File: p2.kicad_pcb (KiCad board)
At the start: 2 copper layers, 66 x 57 mm, 34 parts, among them J1 BARREL_JACK, J2 FLASH_JMP, J3 UART, J4 ALT_POWER, J5 jack-3.5mm-5pin, J6 jack-3.5mm-5pin, J7 jack-3.5mm-5pin, J8 jack-3.5mm-5pin, Q1 IRL540N, Q2 IRL540N, U1 LM1117IMP-33, U2 ESP-12F

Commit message: current state sync
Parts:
- removed C1: 10uF, Capacitors_THT:CP_Radial_Tantal_D5.0mm_P2.50mm
- removed R1, R2, R6, R7: 10k, Resistors_THT:R_Axial_DIN0207_L6.3mm_D2.5mm_P7.62mm_Horizontal
- added LED1: LED, LEDs:LED_D3.0mm_Horizontal_O1.27mm_Z2.0mm, F.Cu at (59.2, 27.6)
- added LED2: LED, LEDs:LED_D3.0mm_Horizontal_O1.27mm_Z2.0mm, F.Cu at (54.1, 27.6)
- added R8: 1k, Resistors_THT:R_Axial_DIN0207_L6.3mm_D2.5mm_P7.62mm_Horizontal, F.Cu at (51.6, 37.8)
- added R9: 1k, Resistors_THT:R_Axial_DIN0207_L6.3mm_D2.5mm_P7.62mm_Horizontal, F.Cu at (54.1, 37.8)
- added RN1: 10k, Resistors_THT:R_Array_SIP5, F.Cu at (38.3, 52.3)
- added U3: Switch, Buttons_Switches_THT:SW_PUSH_6mm, F.Cu at (68.5, 27.1)
- C2: value 10uF -> 10u
- C3, C4: value 100nF -> 100n
- U1: value LM1117IMP-33 -> R-78E3.3-0.5; footprint TO_SOT_Packages_SMD:SOT-223 -> myfootprints:DCDC-Conv_Recom_R-78Exx-0.5
- U2: value ESP-12F -> ESP-12; footprint esp8266:ESP-12E -> esp8266:ESP-12
- moved REF*** 26.7 mm to (68.1, 59.9)
- moved C2 15.9 mm to (42.4, 48.3), turned to 0 degrees
- moved U1 11.7 mm to (53.6, 45.7)
- moved G*** 5.67 mm to (70.6, 39.3)
- moved REF** 5.60 mm to (71.7, 41.6)
- moved J1 1.70 mm to (38.1, 26.0)
- moved J3 1.27 mm to (45.2, 74.6)
- moved R5 1.13 mm to (77.1, 74.6)
- moved R3 1.08 mm to (35.1, 74.6)
- moved REF** 1.08 mm to (38.0, 35.5)
- moved C3 0.63 mm to (33.8, 47.3)
- moved C4 0.63 mm to (55.4, 51.1)
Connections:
- net Net-(D1-Pad2) renamed /pump1
- net Net-(D2-Pad2) renamed /pump2
- net Net-(R3-Pad2) renamed /wifi-sw
- C2 pad 1: /Vcc -> +3V3
- C3 pad 2: /Vcc -> +3V3
- D1 pad 1: /12V -> +12V
- D2 pad 1: /12V -> +12V
- J1 pad 1: /12V -> +12V
- J3 pad 2: /Vcc -> +3V3
- J4 pad 2: /12V -> +12V
- J7 pad 2: /12V -> +12V
- J8 pad 2: /12V -> +12V
- U1 pad 1: GNDREF -> +12V
- U1 pad 2: /Vcc -> GNDREF
- U1 pad 3: /12V -> +3V3
- U2 pad 13: Net-(U2-Pad13) -> /led2
- U2 pad 14: Net-(U2-Pad14) -> /led1
- U2 pad 8: /Vcc -> +3V3
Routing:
- net /12V: track 134.5 -> 0.00 mm
- net +3V3: track 0.00 -> 117.3 mm
- net +12V: track 0.00 -> 100.3 mm
- net /Vcc: track 75.4 -> 0.00 mm
- net /wifi-sw: track 8.12 -> 76.1 mm, vias 0 -> 2
- net /led1: track 0.00 -> 53.4 mm, vias 0 -> 1
- net /led2: track 0.00 -> 47.6 mm, vias 0 -> 1
- net /ctl1: track 64.0 -> 71.0 mm
- net /pump2: track 21.9 -> 16.3 mm
- net GNDREF: track 4.50 -> 0.54 mm
- net Net-(LED1-Pad2): track 0.00 -> 3.59 mm
- net /ctl2: track 59.5 -> 56.7 mm
- net Net-(LED2-Pad2): track 0.00 -> 2.54 mm
- net Net-(Q1-Pad1): track 36.2 -> 38.6 mm
- net /GPIO0: track 24.0 -> 22.1 mm
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- removed copper zone on F.Cu, net /HEAT_Vcc
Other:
- outline, holes or cut-outs redrawn
- board text added: "Gnd"
- board text added: "GndVcc Rx Tx"
- board text added: "Pump1"
- board text added: "Pump2"
- board text added: "Sensor1"
- board text added: "Sensor2"
- board text added: "WaterControl v2 r1.7"
- board text added: "short"
- board text added: "to flash"
- board text removed: "GND"
- board text removed: "Short to flash"
- board text removed: "WaterControl v2 r1.1"

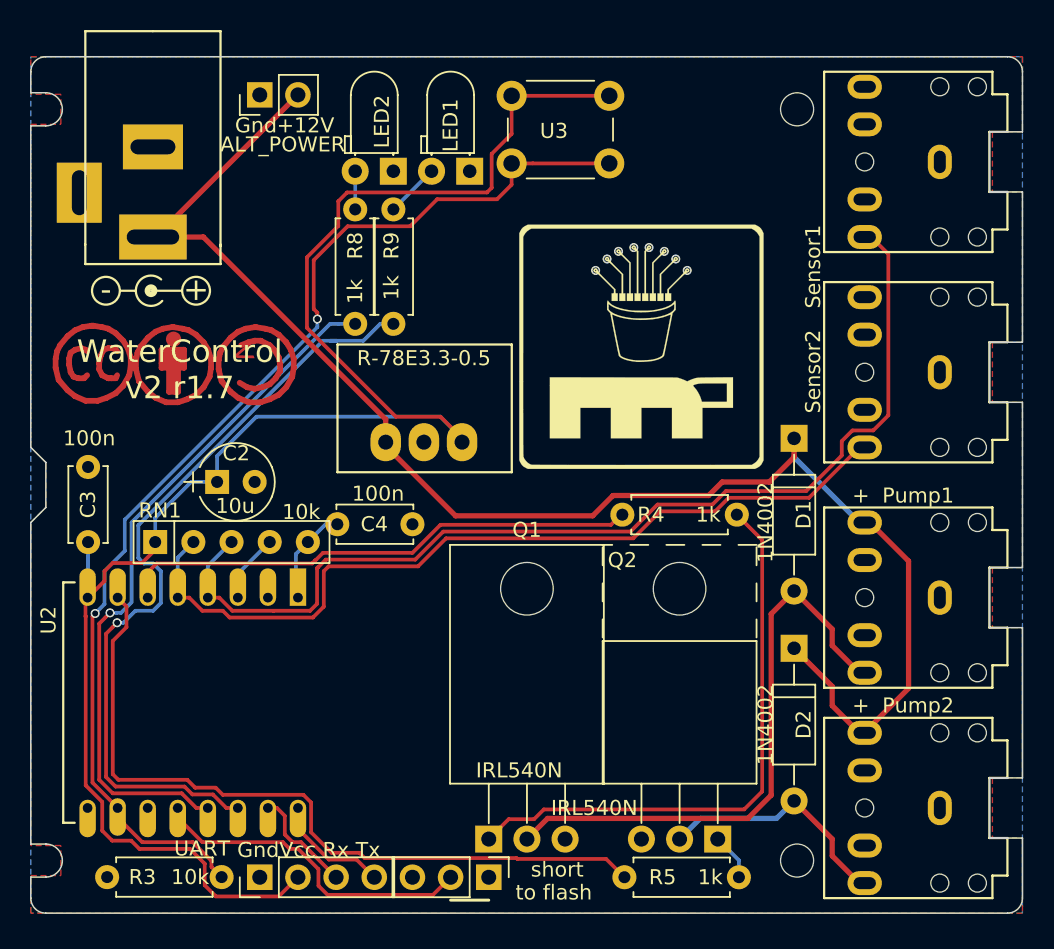
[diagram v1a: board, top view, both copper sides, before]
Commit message: rev4.1 - switched to capacitive sensors by including a multiplexer, added another switch, rotated both.
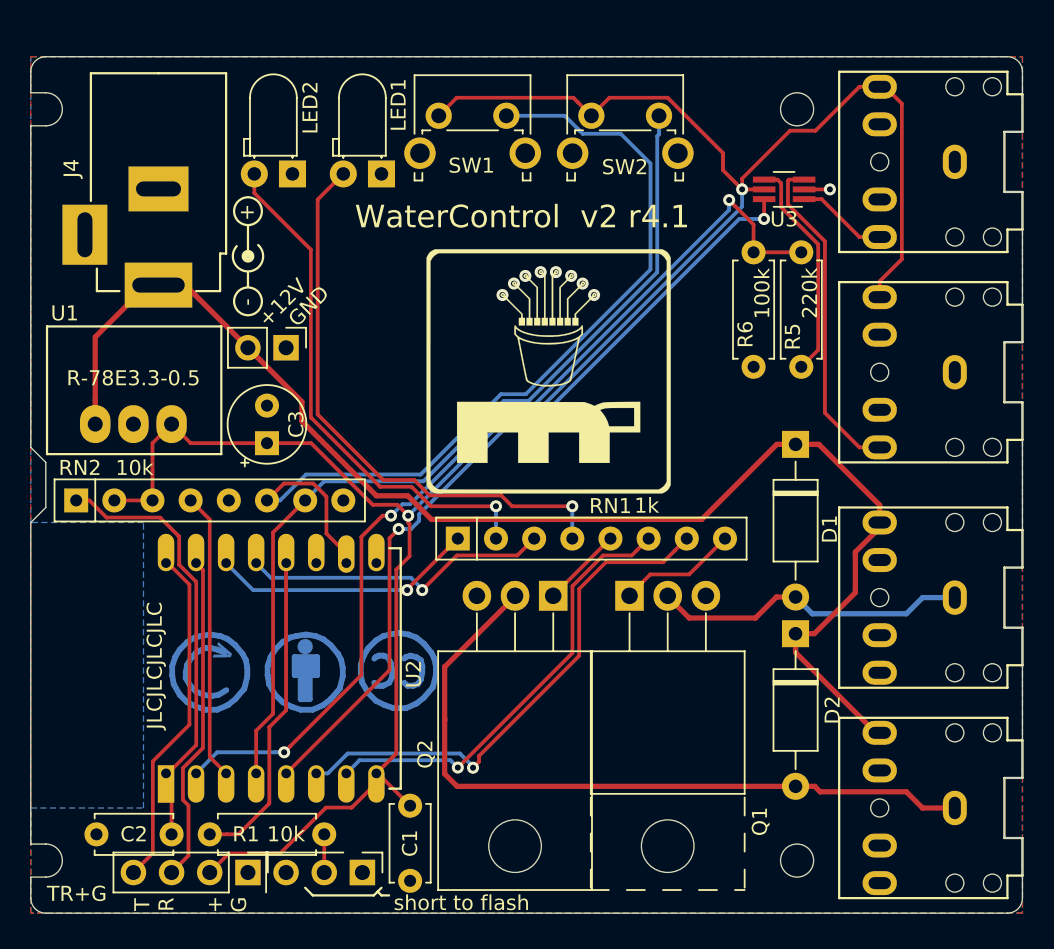
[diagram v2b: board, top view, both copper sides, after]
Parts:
- removed C4: 100n, Capacitors_THT:C_Disc_D5.0mm_W2.5mm_P5.00mm
- removed the G*** at (70.6, 39.3)
- removed R3: 10k, Resistors_THT:R_Axial_DIN0207_L6.3mm_D2.5mm_P7.62mm_Horizontal
- removed R4, R8, R9: 1k, Resistors_THT:R_Axial_DIN0207_L6.3mm_D2.5mm_P7.62mm_Horizontal
- removed the REF** at (34.0, 40.5)
- removed the REF** at (45.0, 40.5)
- removed the REF** at (39.5, 40.5)
- removed the REF** at (71.7, 41.6)
- removed the REF** at (38.0, 35.5)
- removed REF***: OSHW-Logo2_9.8x8mm_SilkScreen, Symbols:OSHW-Logo2_9.8x8mm_SilkScreen
- added C1: 100n, Capacitor_THT:C_Disc_D5.0mm_W2.5mm_P5.00mm, F.Cu at (55.2, 69.8)
- added G***: MR_EDGE_PCBPOT, mylogos:mr_edge_pcbpot, B.Cu at (64.5, 40.9)
- added G***: MR_EDGE_PCBPOT, mylogos:mr_edge_pcbpot, F.Cu at (64.5, 40.9)
- added R1: 10k, Resistor_THT:R_Axial_DIN0207_L6.3mm_D2.5mm_P7.62mm_Horizontal, F.Cu at (41.9, 71.8)
- added R6: 100k, Resistor_THT:R_Axial_DIN0207_L6.3mm_D2.5mm_P7.62mm_Horizontal, F.Cu at (78.1, 40.6)
- added REF**: Symbol_Barrel_Polarity, Symbol:Symbol_Barrel_Polarity, F.Cu at (44.4, 33.3)
- added REF**: Symbol_CC-ShareAlike_CopperTop_Small, Symbol:Symbol_CC-ShareAlike_CopperTop_Small, B.Cu at (41.9, 61.0)
- added REF**: Symbol_CC-Attribution_CopperTop_Small, Symbol:Symbol_CC-Attribution_CopperTop_Small, B.Cu at (48.3, 61.0)
- added REF**: Symbol_CreativeCommons_CopperTop_Type2_Small, Symbol:Symbol_CreativeCommons_CopperTop_Type2_Small, B.Cu at (54.6, 61.0)
- added REF**: OSHW-Logo2_9.8x8mm_SilkScreen, Symbol:OSHW-Logo2_9.8x8mm_SilkScreen, B.Cu at (46.5, 33.7)
- added RN2: 10k, myfootprints:ResistorArrayx4-18726345, F.Cu at (33.0, 49.5)
- added SW1: SW_Push, Button_Switch_THT:SW_Tactile_SPST_Angled_PTS645Vx58-2LFS, F.Cu at (57.1, 23.9)
- added SW2: SW_Push, Button_Switch_THT:SW_Tactile_SPST_Angled_PTS645Vx58-2LFS, F.Cu at (67.3, 23.9)
- C2: value 10u -> 100n; footprint Capacitors_THT:CP_Radial_Tantal_D5.0mm_P2.50mm -> Capacitor_THT:C_Disc_D5.0mm_W2.5mm_P5.00mm
- C3: value 100n -> 10u; footprint Capacitors_THT:C_Disc_D5.0mm_W2.5mm_P5.00mm -> Capacitor_THT:CP_Radial_Tantal_D5.0mm_P2.50mm
- D1, D2: footprint Diodes_THT:D_A-405_P10.16mm_Horizontal -> Diode_THT:D_A-405_P10.16mm_Horizontal
- J1: value BARREL_JACK -> FLASH_JMP; footprint myfootprints:Barrel_Jack_5.5_2.1mm -> myfootprints:PinHeader_2.54mm_1x3_short
- J2: value FLASH_JMP -> UART; footprint Pin_Headers:Pin_Header_Straight_1x03_Pitch2.54mm -> Connector_PinHeader_2.54mm:PinHeader_1x04_P2.54mm_Vertical
- J3: value UART -> ALT_Pwr; footprint Pin_Headers:Pin_Header_Straight_1x04_Pitch2.54mm -> Connector_PinHeader_2.54mm:PinHeader_1x02_P2.54mm_Vertical
- J4: value ALT_POWER -> BARREL_JACK; footprint Pin_Headers:Pin_Header_Straight_1x02_Pitch2.54mm -> myfootprints:Barrel_Jack_5.5_2.1mm
- LED1, LED2: footprint LEDs:LED_D3.0mm_Horizontal_O1.27mm_Z2.0mm -> LED_THT:LED_D3.0mm_Horizontal_O1.27mm_Z2.0mm_Clear
- Q1: footprint TO_SOT_Packages_THT:TO-220_Horizontal -> Package_TO_SOT_THT:TO-220-3_Horizontal_TabUp
- Q2: footprint TO_SOT_Packages_THT:TO-220_Horizontal_Reversed -> Package_TO_SOT_THT:TO-220-3_Horizontal_TabDown
- R5: value 1k -> 220k; footprint Resistors_THT:R_Axial_DIN0207_L6.3mm_D2.5mm_P7.62mm_Horizontal -> Resistor_THT:R_Axial_DIN0207_L6.3mm_D2.5mm_P7.62mm_Horizontal
- RN1: value 10k -> 1k; footprint Resistors_THT:R_Array_SIP5 -> myfootprints:ResistorArrayx4-27185436
- U2: footprint esp8266:ESP-12 -> ESP8266:ESP-12
- U3: value Switch -> 74LVC1G3157; footprint Buttons_Switches_THT:SW_PUSH_6mm -> Package_TO_SOT_SMD:SOT-363_SC-70-6_Handsoldering
- moved J1 50.3 mm to (52.1, 74.3)
- moved R5 41.8 mm to (81.3, 33.0), turned to 270 degrees
- moved J3 35.3 mm to (47.0, 39.4), turned to 270 degrees
- moved C2 23.6 mm to (39.4, 71.8), turned to 180 degrees
- moved RN1 20.1 mm to (58.4, 52.1)
- moved Q2 19.5 mm to (64.8, 55.9)
- moved U1 19.4 mm to (34.3, 44.5)
- moved Q1 18.7 mm to (69.8, 55.9)
- moved J2 16.0 mm to (44.5, 74.3)
- moved U2 14.6 mm to (39.0, 67.7), turned to 90 degrees
- moved J5 14.0 mm to (91.5, 41.0)
- moved J6 14.0 mm to (91.5, 27.0)
- moved C3 12.0 mm to (45.7, 45.7), turned to 90 degrees
- moved U3 11.8 mm to (80.1, 28.8)
- moved J4 9.20 mm to (38.5, 28.8), turned to 270 degrees
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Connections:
- C2 pad 1: +3V3 -> /10k_to_3v3_1
- C2 pad 2: GNDREF -> GND
- C3 pad 1: GNDREF -> +3V3
- C3 pad 2: +3V3 -> GND
- D1 pad 2: /pump1 -> Net-(D1-Pad2)
- D2 pad 2: /pump2 -> Net-(D2-Pad2)
- J1 pad 1: +12V -> GND
- J1 pad 2: GNDREF -> Net-(J1-Pad2)
- J2 pad 1: GNDREF -> GND
- J2 pad 2: /GPIO0 -> +3V3
- J2 pad 3: Net-(J2-Pad3) -> /RXD0
- J3 pad 1: GNDREF -> GND
- J3 pad 2: +3V3 -> +12V
- J4 pad 1: GNDREF -> +12V
- J4 pad 2: +12V -> Net-(J4-Pad2)
- J5 pad 1: Net-(J5-Pad1) -> GND
- J5 pad 2: GNDREF -> +3V3
- J5 pad 3: /ctl1 -> Net-(J5-Pad3)
- J6 pad 1: Net-(J6-Pad1) -> GND
- J6 pad 2: GNDREF -> +3V3
- J6 pad 3: /ctl2 -> Net-(J6-Pad3)
- J7 pad 1: Net-(J7-Pad1) -> Net-(D1-Pad2)
- J7 pad 3: /pump1 -> Net-(J7-Pad3)
- J8 pad 1: Net-(J8-Pad1) -> Net-(D2-Pad2)
- J8 pad 3: /pump2 -> Net-(J8-Pad3)
- LED1 pad 1: GNDREF -> GND
- LED1 pad 2: Net-(LED1-Pad2) -> /led1
- LED2 pad 1: GNDREF -> GND
- LED2 pad 2: Net-(LED2-Pad2) -> /led2
- Q1 pad 1: Net-(Q1-Pad1) -> /pump_ctl_1
- Q1 pad 2: /pump1 -> Net-(D1-Pad2)
- Q1 pad 3: GNDREF -> GND
- Q2 pad 1: Net-(Q2-Pad1) -> /pump_ctl_2
- Q2 pad 2: /pump2 -> Net-(D2-Pad2)
- Q2 pad 3: GNDREF -> GND
- R5 pad 1: Net-(Q2-Pad1) -> /sensor_in
- R5 pad 2: /ctl4 -> Net-(R5-Pad2)
- RN1 pad 1: +3V3 -> Net-(RN1-Pad1)
- RN1 pad 2: /ctl2 -> Net-(RN1-Pad2)
- RN1 pad 3: /ctl1 -> Net-(RN1-Pad3)
- RN1 pad 5: Net-(C4-Pad2) -> /pump_ctl_2
- U1 pad 2: GNDREF -> GND
- U2 pad 1: Net-(C4-Pad2) -> /10k_to_3v3_1
- U2 pad 10: /wifi-sw -> /10k_to_gnd_1
- U2 pad 12: /GPIO0 -> /GPIO_0_Flash
- U2 pad 13: /led2 -> Net-(RN1-Pad1)
- U2 pad 14: /led1 -> Net-(RN1-Pad2)
- U2 pad 2: Net-(U2-Pad2) -> /sensor_in
- U2 pad 3: Net-(RN1-Pad4) -> /10k_to_3v3_2
- U2 pad 4: /ctl1 -> /10k_to_gnd_2
- U2 pad 5: /ctl2 -> /sensor_switch
- U2 pad 6: /ctl3 -> Net-(RN1-Pad3)
- U2 pad 7: /ctl4 -> Net-(RN1-Pad4)
- U2 pad 9: GNDREF -> GND
- U3 pad 1: /wifi-sw -> Net-(J6-Pad3)
- U3 pad 2: +3V3 -> GND
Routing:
- net /wifi-sw: track 76.1 -> 0.00 mm, vias 2 -> 0
- net /ctl1: track 71.0 -> 0.00 mm
- net /sensor_in: track 0.00 -> 64.4 mm, vias 0 -> 3
- net /10k_to_gnd_1: track 0.00 -> 59.8 mm
- net /10k_to_gnd_2: track 0.00 -> 59.7 mm
- net /ctl2: track 56.7 -> 0.00 mm
- net /sensor_switch: track 0.00 -> 53.8 mm, vias 0 -> 2
- net /ctl4: track 50.4 -> 0.00 mm
- net Net-(D2-Pad2): track 0.00 -> 48.8 mm
- net /pump1: track 39.3 -> 0.00 mm
- net Net-(Q1-Pad1): track 38.6 -> 0.00 mm
- net /ctl3: track 35.1 -> 0.00 mm
- net Net-(RN1-Pad3): track 0.00 -> 34.8 mm, vias 0 -> 1
- net +3V3: track 117.3 -> 149.1 mm, vias 0 -> 2
- net /10k_to_3v3_1: track 0.00 -> 29.7 mm
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- added copper zone on B.Cu, net GND
- removed copper zone on B.Cu, net GNDREF
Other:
- outline, holes or cut-outs redrawn
- net class Default: via_dia 0.6 -> 0.8
- net class pwr: via_dia 0.7 -> 0.8
- rule pad_to_mask_clearance: 0 -> 0.051
- board text added: "GND"
- board text added: "JLCJLCJLCJLC"
- board text added: "T R + G"
- board text added: "TR+G"
- board text added: "WaterControl v2 r4.1"
- board text added: "short to flash"
- board text removed: "Gnd"
- board text removed: "GndVcc Rx Tx"
- board text removed: "Pump1"
- board text removed: "Pump2"
- board text removed: "Sensor1"
- board text removed: "Sensor2"
- board text removed: "UART"
- board text removed: "WaterControl v2 r1.7"
- board text removed: "designed with"
- board text removed: "short"
- board text removed: "to flash"
